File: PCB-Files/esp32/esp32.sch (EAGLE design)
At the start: 20 parts, among them SW1 SPST_TACT-KMR2, SW2 SPST_TACT-KMR2, X2 ESP32_WROOM32_SKINNY

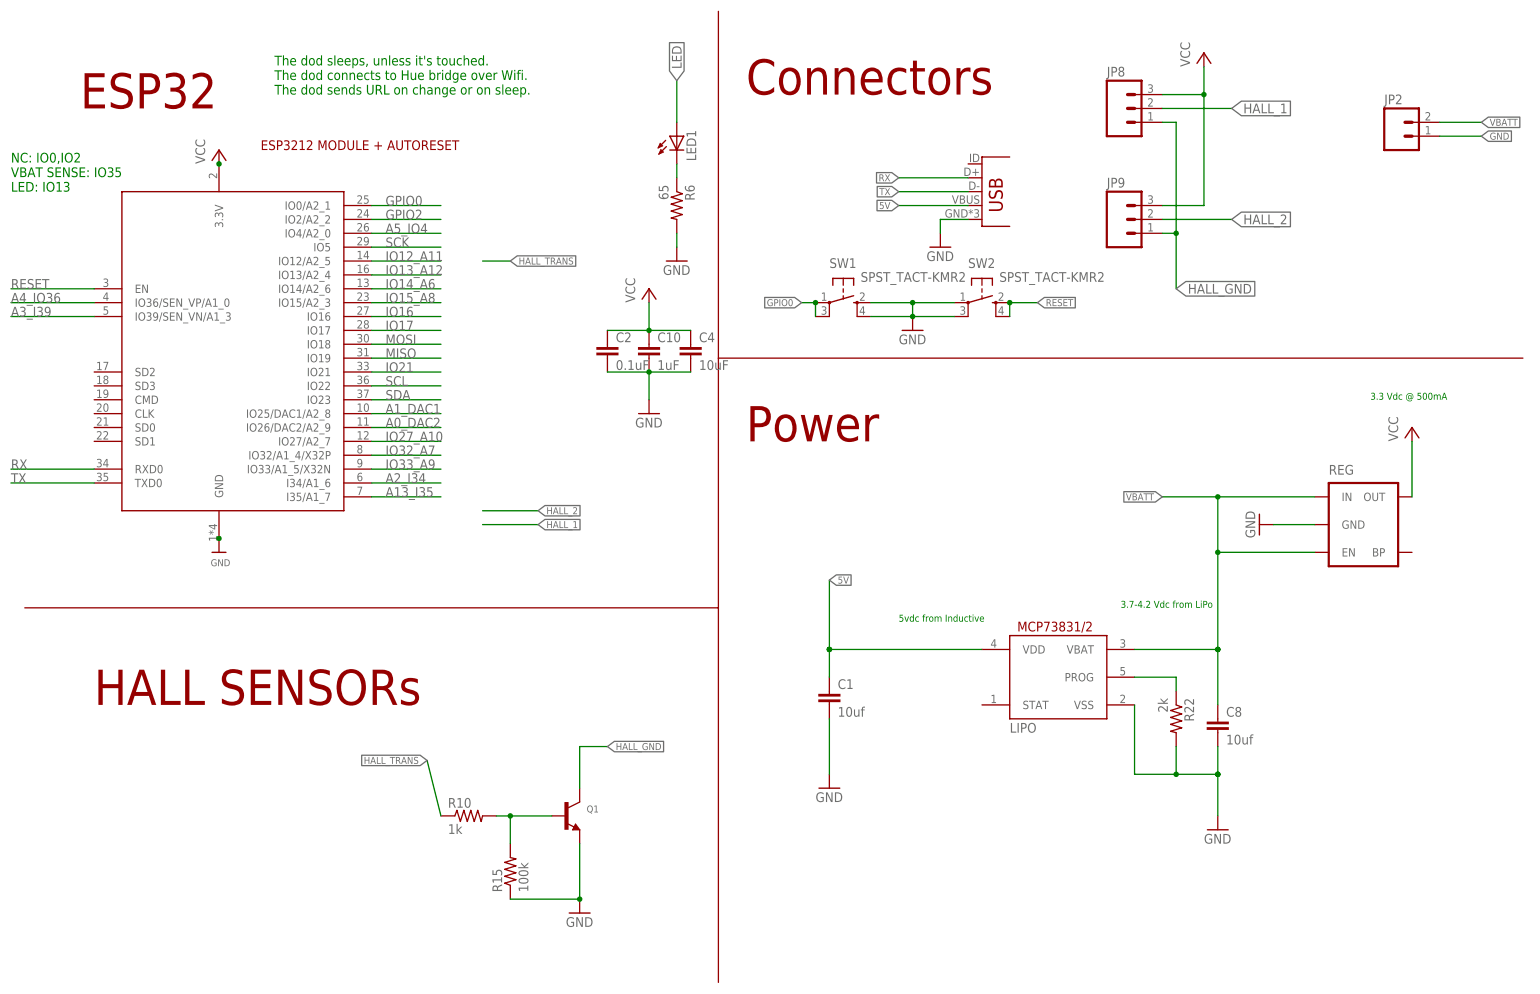
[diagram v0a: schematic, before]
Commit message: rounded 4-side for class
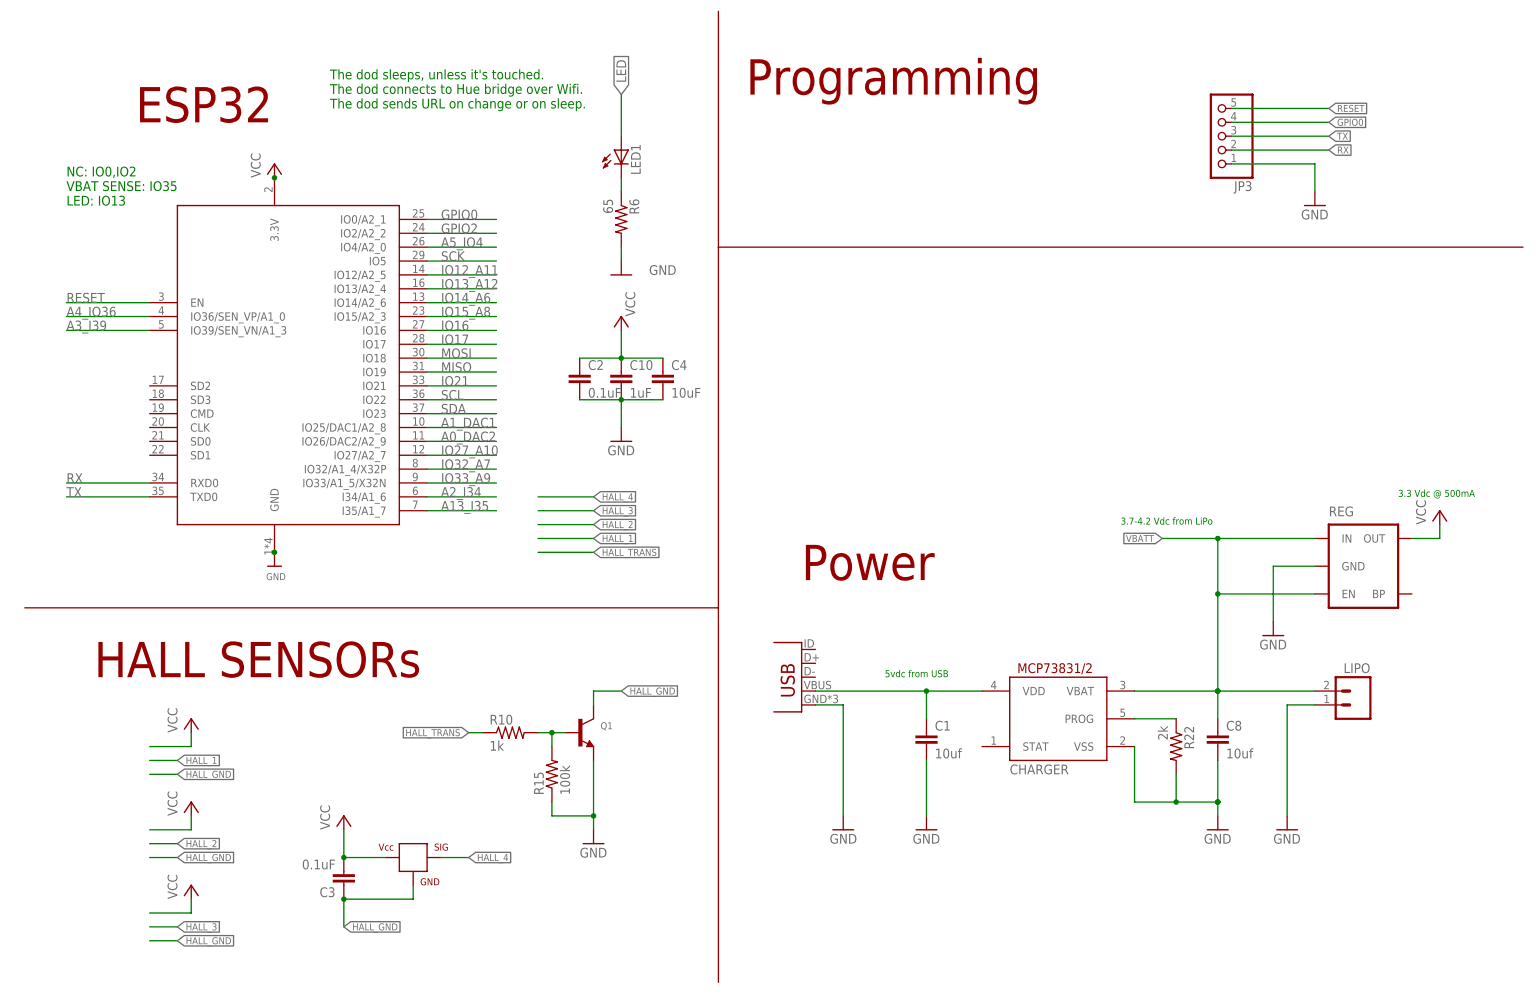
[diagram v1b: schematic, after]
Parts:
- removed JP2: (no value), SparkFun:M02
- removed JP8, JP9: (no value), SparkFun:M03PTH
- removed SW1, SW2: SPST_TACT-KMR2, adafruit:SPST_TACT-KMR2
- added C3: 0.1uF, SparkFun:CAP0603-CAP
- added CHARGER: MCP73831/OT, adafruit:MCP73831/OT
- added HALL: HALLEFFECT-A1326, Andy_Sigler:HALLEFFECT-A1326
- added JP3: (no value), pinhead:PINHD-1X55X2MM
- LIPO: value MCP73831/OT -> (none); device adafruit:MCP73831/OT -> SparkFun:M02
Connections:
- removed net HALL_1: JP8.2
- removed net HALL_2: JP9.2
- new net HALL_4: HALL.SIG
- net 5V: now also CHARGER.VDD; no longer LIPO.VDD
- net GND: now also CHARGER.VSS, JP3.1, LIPO.1; no longer JP2.1, LIPO.VSS, SW1.S, SW1.S1, SW2.P, SW2.P1
- net GPIO0: now also JP3.4; no longer SW1.P, SW1.P1
- net HALL_GND: now also C3.1, HALL.GND; no longer JP8.1, JP9.1
- net N$2: now also CHARGER.PROG; no longer LIPO.PROG
- net RESET: now also JP3.5; no longer SW2.S, SW2.S1
- net RX: now also JP3.2; no longer JP1.D+
- net TX: now also JP3.3; no longer JP1.D-
- net VBATT: now also CHARGER.VBAT, LIPO.2; no longer JP2.2, LIPO.VBAT
- net VCC: now also C3.2, HALL.VCC; no longer JP8.3, JP9.3
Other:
- note added: "5vdc from USB"
- note added: "Programming"
- note removed: "5vdc from Inductive"
- note removed: "Connectors"
- note removed: "ESP3212 MODULE + AUTORESET"
- moved on the sheet: C1, C10, C2, C4, C8, LED1, Q1, R10, R15, R22, R6, REG
